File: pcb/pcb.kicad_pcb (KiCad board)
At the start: 2 copper layers, 26.2 x 19 mm, 5 parts, among them J1 PINHD_1x5_Female

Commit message: pcb stuff
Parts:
- removed CH1: choc_v1_SW_HS, PCM_marbastlib-choc:SW_choc_v1_HS_CPG135001S30_1u
- removed D1: 1N4148, PCM_Diode_THT_AKL:D_DO-35_SOD27_P7.62mm_Horizontal
- removed J1: PINHD_1x5_Female, PCM_4ms_Connector:Pins_1x05_2.54mm_TH
- removed LED1: choc_SK6812MINI-E, PCM_marbastlib-choc:LED_choc_6028R
- removed R1: 500, PCM_4ms_Resistor:R_0603
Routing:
- net Net-(LED1-VDD): track 40.0 -> 0.00 mm
- net Net-(D1-A): track 21.0 -> 0.00 mm
- net Net-(D1-K): track 19.4 -> 0.00 mm
- net Net-(LED1-DIN): track 11.1 -> 0.00 mm, vias 1 -> 0
- net Net-(LED1-VSS): track 4.19 -> 0.00 mm
- net Net-(LED1-DOUT): track 3.02 -> 0.00 mm
- net Net-(J1-Pad5): track 2.29 -> 0.00 mm
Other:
- board size 26.2 x 19 mm -> 36.5 x 57 mm

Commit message: some schematic changes
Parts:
- added J1: Input, PCM_SparkFun-Connector:JST_1x08_P1.25mm_Locking_Horizontal_SMD, F.Cu at (228.1, 38.5)
- added J2: Output, PCM_SparkFun-Connector:JST_1x08_P1.25mm_Locking_Horizontal_SMD, F.Cu at (247.8, 88.2)
- added JMP_BTN1: ~, PCM_SparkFun-Jumper:Jumper_2_NO_NoSilk, F.Cu at (231.4, 48.0)
- added JMP_BTN2: ~, PCM_SparkFun-Jumper:Jumper_2_NO_NoSilk, F.Cu at (231.4, 50.7)
- added JMP_BTN3: ~, PCM_SparkFun-Jumper:Jumper_2_NO_NoSilk, F.Cu at (234.3, 48.0)
- added JMP_BTN4: ~, PCM_SparkFun-Jumper:Jumper_2_NO_NoSilk, F.Cu at (234.3, 50.7)
- added JMP_BTN5: ~, PCM_SparkFun-Jumper:Jumper_2_NO_NoSilk, F.Cu at (237.2, 48.0)
- added JMP_BTN6: ~, PCM_SparkFun-Jumper:Jumper_2_NO_NoSilk, F.Cu at (237.2, 50.7)
- added JMP_BTN7: ~, PCM_SparkFun-Jumper:Jumper_2_NO_NoSilk, F.Cu at (240.2, 48.0)
- added JMP_BTN8: ~, PCM_SparkFun-Jumper:Jumper_2_NO_NoSilk, F.Cu at (240.2, 50.7)
- added USB1: HRO-TYPE-C-31-M-12, extern:HRO-TYPE-C-31-M-12-HandSoldering, F.Cu at (256.2, 56.0)
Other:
- board size 36.5 x 57 mm -> 41.3 x 62.7 mm

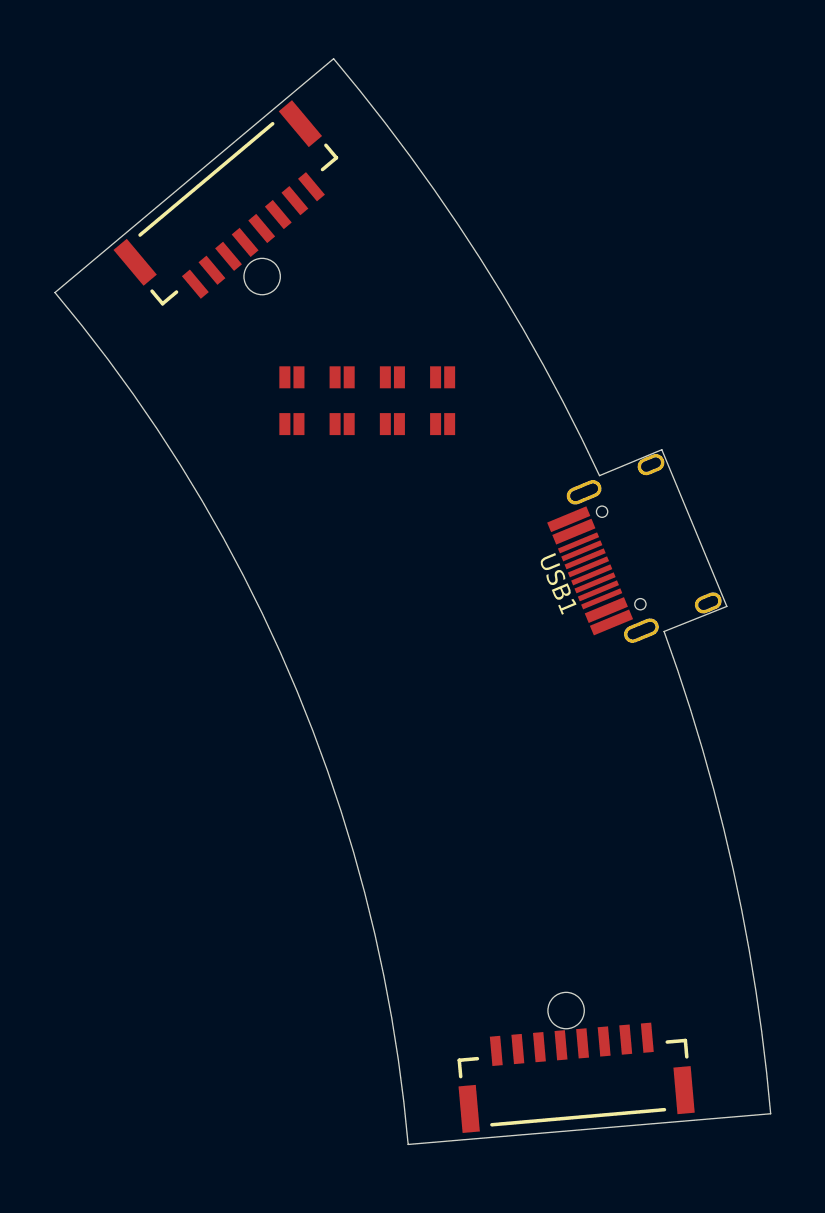
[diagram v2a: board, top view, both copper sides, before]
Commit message: making a curved pcb was a mistake, why did i angled this
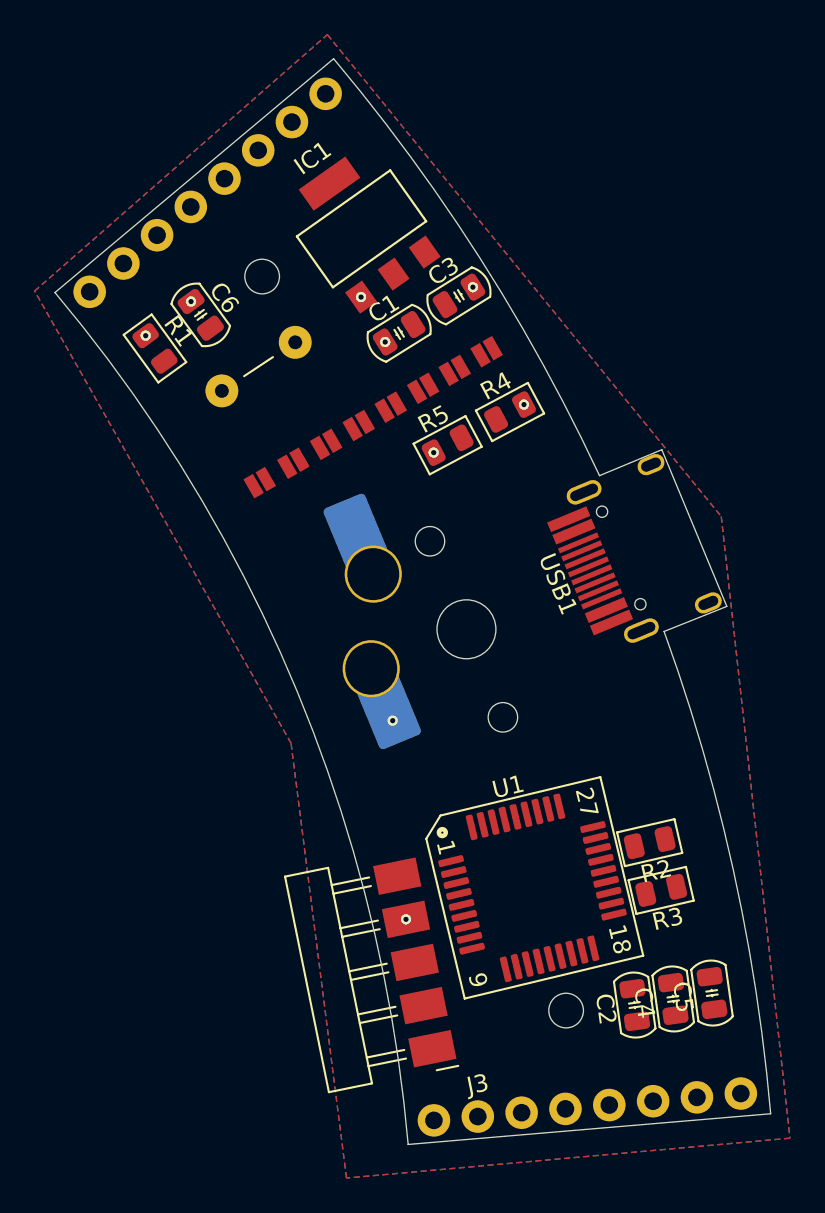
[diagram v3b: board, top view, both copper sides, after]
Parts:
- added C1: 10uF, PCM_Capacitor_SMD_Handsoldering_AKL:C_0805_2012Metric, F.Cu at (237.6, 45.4)
- added C2: 100uF, PCM_Capacitor_SMD_Handsoldering_AKL:C_0805_2012Metric, F.Cu at (251.2, 84.2)
- added C3: 1uF, PCM_Capacitor_SMD_Handsoldering_AKL:C_0805_2012Metric, F.Cu at (241.1, 43.3)
- added C4: 100uF, PCM_Capacitor_SMD_Handsoldering_AKL:C_0805_2012Metric, F.Cu at (253.5, 83.9)
- added C5: 100uF, PCM_Capacitor_SMD_Handsoldering_AKL:C_0805_2012Metric, F.Cu at (255.7, 83.5)
- added C6: 100uF, PCM_Capacitor_SMD_Handsoldering_AKL:C_0805_2012Metric, F.Cu at (226.2, 44.4)
- added CH1: choc_v1_SW_HS, PCM_marbastlib-choc:SW_choc_v1_HS_CPG135001S30_1u, B.Cu at (241.5, 62.5)
- added IC1: LD1117-3.3V-SOT223, PCM_4ms_Package_SOT:SOT223, F.Cu at (235.5, 39.4)
- added J3: PinHeader_01x05_P2.54mm_Horizontal_SMD, PCM_fab:PinHeader_01x05_P2.54mm_Horizontal_SMD, F.Cu at (239.6, 86.7)
- added JP1: JUP_P5.08mm, PCM_SL_Jumpers:JUP_P5.08mm, F.Cu at (229.5, 47.4)
- added R1: 10k, PCM_Resistor_SMD_AKL:R_0805_2012Metric, F.Cu at (223.5, 46.3)
- added R2: 22, PCM_Resistor_SMD_AKL:R_0805_2012Metric, F.Cu at (252.1, 74.8)
- added R3: 22, PCM_Resistor_SMD_AKL:R_0805_2012Metric, F.Cu at (252.8, 77.6)
- added R4: 5.1k, PCM_Resistor_SMD_AKL:R_0805_2012Metric, F.Cu at (244.0, 50.0)
- added R5: 5.1k, PCM_Resistor_SMD_AKL:R_0805_2012Metric, F.Cu at (240.4, 51.9)
- added U1: ~, PCM_Package_QFP_AKL:LQFP-36_7x7mm_P0.65mm, F.Cu at (245.3, 77.5)
- J1: footprint PCM_SparkFun-Connector:JST_1x08_P1.25mm_Locking_Horizontal_SMD -> PCM_SparkFun-Connector:1x08_P2.54mm
- J2: footprint PCM_SparkFun-Connector:JST_1x08_P1.25mm_Locking_Horizontal_SMD -> PCM_SparkFun-Connector:1x08_P2.54mm; moved to B.Cu
- moved JMP_BTN1 11.3 mm to (242.7, 46.5), turned to -150 degrees
- moved JMP_BTN8 11.1 mm to (229.6, 54.1), turned to 30 degrees
- moved JMP_BTN7 9.94 mm to (231.5, 52.9), turned to 30 degrees
- moved JMP_BTN2 9.89 mm to (240.8, 47.6), turned to 30 degrees
- moved J2 9.67 mm to (257.4, 89.3), turned to -175 degrees
- moved J1 8.65 mm to (233.4, 31.6)
- moved JMP_BTN3 4.72 mm to (239.0, 48.6), turned to 30 degrees
- moved JMP_BTN6 4.00 mm to (233.4, 51.8), turned to 30 degrees
- moved JMP_BTN5 3.39 mm to (235.3, 50.8), turned to 30 degrees
- moved JMP_BTN4 2.97 mm to (237.2, 49.7), turned to 30 degrees
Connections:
- JMP_BTN1 pad 1: /BTN1 -> Net-(JMP_BTN1-A)
- JMP_BTN2 pad 2: /BTN1 -> Net-(JMP_BTN1-A)
- JMP_BTN3 pad 2: /BTN1 -> Net-(JMP_BTN1-A)
- JMP_BTN4 pad 2: /BTN1 -> Net-(JMP_BTN1-A)
- JMP_BTN5 pad 2: /BTN1 -> Net-(JMP_BTN1-A)
- JMP_BTN6 pad 2: /BTN1 -> Net-(JMP_BTN1-A)
- JMP_BTN7 pad 2: /BTN1 -> Net-(JMP_BTN1-A)
- JMP_BTN8 pad 2: /BTN1 -> Net-(JMP_BTN1-A)
- USB1 pad 1: unconnected-(USB1-GND-Pad1) -> GND
- USB1 pad 10: unconnected-(USB1-CC2-Pad10) -> Net-(USB1-CC2)
- USB1 pad 11: unconnected-(USB1-VBUS-Pad11) -> 5V
- USB1 pad 12: unconnected-(USB1-GND-Pad12) -> GND
- USB1 pad 13: unconnected-(USB1-SHIELD-Pad13) -> GND
- USB1 pad 2: unconnected-(USB1-VBUS-Pad2) -> 5V
- USB1 pad 4: unconnected-(USB1-CC1-Pad4) -> Net-(USB1-CC1)
- USB1 pad 5: unconnected-(USB1-DN2-Pad5) -> /D-
- USB1 pad 6: unconnected-(USB1-DP1-Pad6) -> /D+
- USB1 pad 7: unconnected-(USB1-DN1-Pad7) -> /D-
- USB1 pad 8: unconnected-(USB1-DP2-Pad8) -> /D+
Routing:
- net GND: vias 0 -> 8
- net +3.3V: vias 0 -> 1
- added copper zone on F.Cu, net +3.3V
- added copper zone on B.Cu, net GND
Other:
- outline, holes or cut-outs redrawn

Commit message: pcb revise
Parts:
- J2: moved to F.Cu
- moved C3 156.3 mm to (119.4, 141.5), turned to 0 degrees
- moved C6 150.8 mm to (119.4, 150.8), turned to 0 degrees
- moved C5 150.6 mm to (119.4, 147.7), turned to 0 degrees
- moved J1 149.9 mm to (118.8, 128.3), turned to 0 degrees
- moved C1 148.4 mm to (119.4, 135.2), turned to 0 degrees
- moved C4 147.1 mm to (119.4, 144.6), turned to 0 degrees
- moved JP1 145.7 mm to (126.2, 150.1), turned to 0 degrees
- moved J2 145.0 mm to (118.8, 131.9), turned to 0 degrees
- moved C2 142.5 mm to (119.4, 138.4), turned to 0 degrees
- moved R4 138.9 mm to (141.5, 143.8), turned to 0 degrees
- moved R5 137.1 mm to (141.5, 146.9), turned to 0 degrees
- moved J3 125.4 mm to (124.2, 136.0), turned to 0 degrees
- moved R1 125.0 mm to (141.5, 140.6), turned to 0 degrees
- moved R3 115.5 mm to (138.5, 94.5), turned to 180 degrees
- moved R2 115.0 mm to (138.5, 92.5), turned to 180 degrees
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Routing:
- net Net-(JMP_BTN1-A): track 0.00 -> 47.5 mm, vias 0 -> 10
- net /D-: track 0.00 -> 13.9 mm
- net /D+: track 0.00 -> 13.2 mm
- net Net-(U1-PA12): track 0.00 -> 5.15 mm
- net Net-(U1-PA11): track 0.00 -> 3.49 mm
- net GND: vias 8 -> 0
- net +3.3V: vias 1 -> 0
- removed copper zone on F.Cu, net +3.3V
- removed copper zone on B.Cu, net GND
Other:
- board size 41.3 x 62.7 mm -> 65.8 x 28.6 mm

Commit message: pcb drc factoring pending
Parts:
- added SW1: Push_Button, Button_Switch_THT:SW_PUSH_6mm, F.Cu at (165.0, 93.5)
- J3: footprint PCM_fab:PinHeader_01x05_P2.54mm_Horizontal_SMD -> PCM_fab:PinHeader_01x05_P2.54mm_Vertical_THT_D1.4mm
- moved C3 61.4 mm to (172.4, 110.5)
- moved C1 61.3 mm to (174.0, 107.2), turned to 180 degrees
- moved J2 60.1 mm to (175.8, 112.8), turned to 73 degrees
- moved R5 57.8 mm to (156.8, 91.1)
- moved R1 57.4 mm to (174.8, 93.8), turned to 180 degrees
- moved C5 55.9 mm to (131.9, 93.2), turned to 90 degrees
- moved JP1 54.8 mm to (124.4, 95.3), turned to 180 degrees
- moved R4 52.5 mm to (143.2, 91.3)
- moved C6 52.5 mm to (124.6, 98.6)
- moved C4 52.0 mm to (129.5, 93.6), turned to 90 degrees
- moved C2 47.9 mm to (134.4, 92.9), turned to 90 degrees
- moved J3 26.6 mm to (127.6, 109.6), turned to 90 degrees
- moved J1 16.5 mm to (124.3, 112.8), turned to 108 degrees
- moved IC1 11.0 mm to (168.2, 106.9), turned to 180 degrees
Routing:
- net +3.3V: track 0.00 -> 95.7 mm, vias 0 -> 10
- net /BTN8: track 0.00 -> 84.8 mm
- net /BTN7: track 0.00 -> 75.3 mm, vias 0 -> 1
- net /BTN2: track 0.00 -> 73.7 mm, vias 0 -> 2
- net /BTN3: track 0.00 -> 73.6 mm, vias 0 -> 2
- net /BTN6: track 0.00 -> 72.6 mm
- net /BTN5: track 0.00 -> 72.0 mm
- net /BTN4: track 0.00 -> 70.8 mm
- net GND: track 0.00 -> 55.7 mm, vias 0 -> 13
- net Net-(U1-PB8-BOOT0): track 0.00 -> 52.3 mm, vias 0 -> 1
- net 5V: track 0.00 -> 49.2 mm, vias 0 -> 2
- net /BTN1: track 0.00 -> 29.4 mm
- net /RST: track 0.00 -> 27.6 mm, vias 0 -> 2
- net /SWDIO: track 0.00 -> 19.2 mm, vias 0 -> 1
- net /SWCLK: track 0.00 -> 13.6 mm, vias 0 -> 1
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- added copper zone on B.Cu, net +3.3V
- added copper zone on B.Cu, net GND
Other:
- board text added: "${REFERENCE}"
- board text added: "18x17 spacing"
- board text added: "19.05 spacing"
- board text added: "LED"

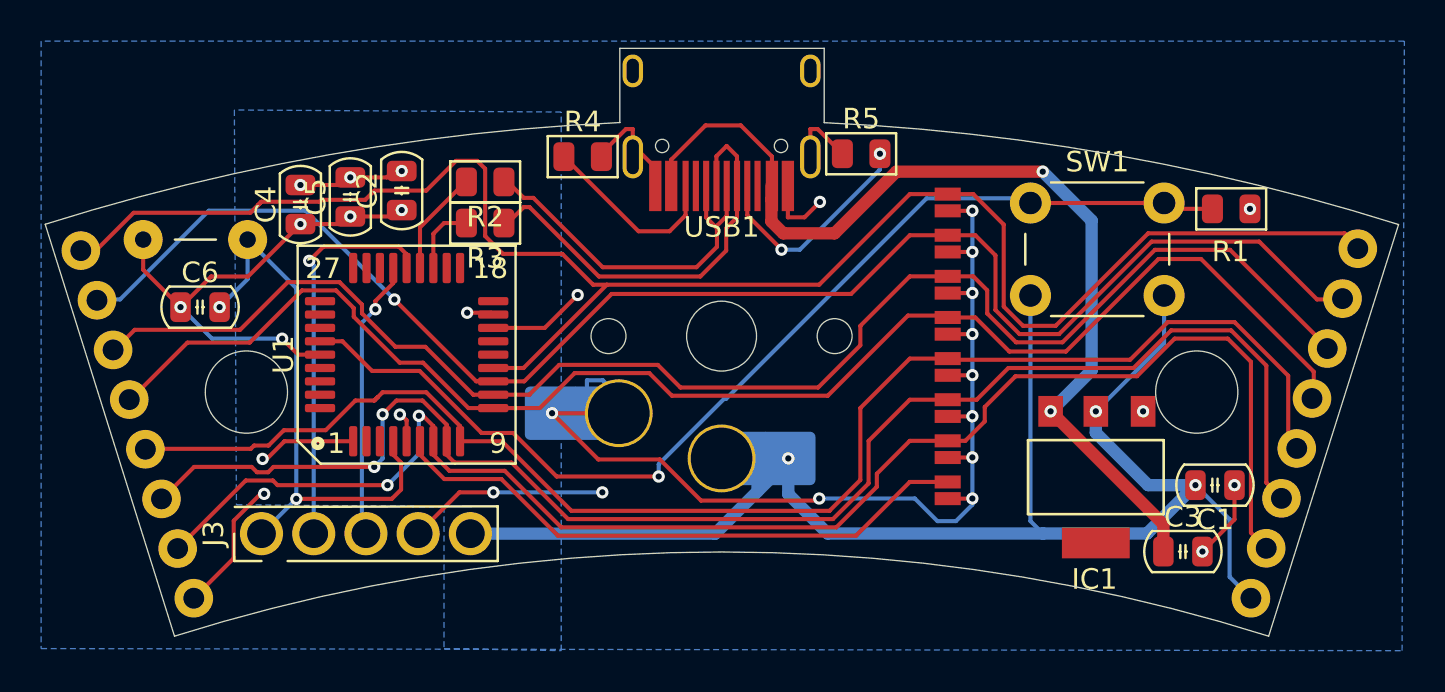
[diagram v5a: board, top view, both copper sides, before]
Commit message: drc resolved pcb ordered
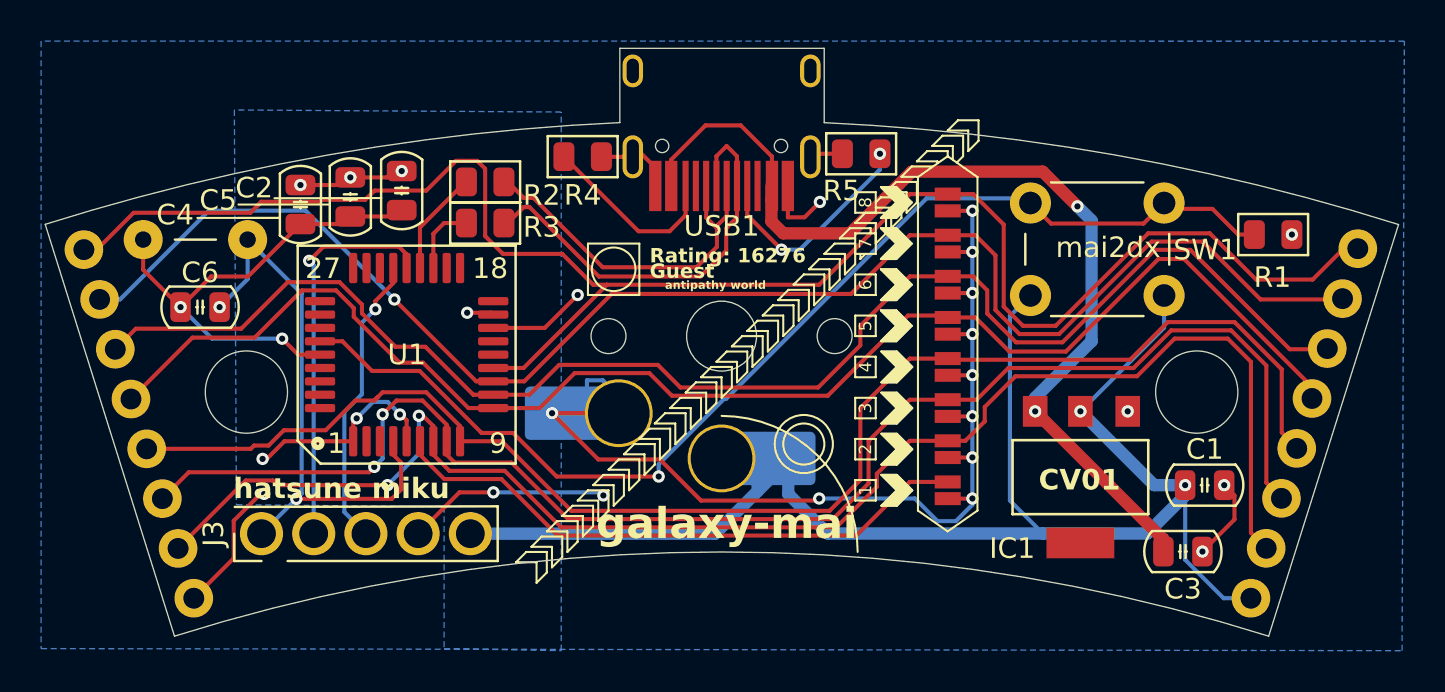
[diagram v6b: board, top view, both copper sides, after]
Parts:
- CH1: value choc_v1_SW_HS -> choc_v2_SW_HS
- moved R1 2.39 mm to (176.8, 95.1)
- moved IC1 0.75 mm to (167.5, 106.9)
- moved C1 0.50 mm to (173.5, 107.2)
- turned J1 to 107.5 degrees
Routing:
- net +3.3V: track 95.7 -> 101.2 mm
- net Net-(U1-PB8-BOOT0): track 52.3 -> 55.7 mm
- net GND: track 55.7 -> 53.0 mm, vias 13 -> 10
- net /BTN8: track 84.8 -> 86.0 mm
- net /SWCLK: track 13.6 -> 14.3 mm
- net 5V: track 49.2 -> 49.8 mm
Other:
- board text added: "1"
- board text added: "2"
- board text added: "3"
- board text added: "4"
- board text added: "5"
- board text added: "6"
- board text added: "7"
- board text added: "8"
- board text added: "As you can probably see... there is no stars on this pcb... i tried... though"
- board text added: "CV01"
- board text added: "Guest"
- board text added: "Rating: 16276"
- board text added: "antipathy world"
- board text added: "galaxy-mai"
- board text added: "hatsune miku"
- board text added: "mai2dx"
- board text added: "short the pads per key..."
